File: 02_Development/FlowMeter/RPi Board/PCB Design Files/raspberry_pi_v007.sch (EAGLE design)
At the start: 136 parts, among them J3 277-2419-ND, J5 POWER_JACK, J7 277-2419-ND, J8 277-2419-ND, J9 277-2419-ND, P1 SPL006-007, P2 SPL006-007, P3 SPL006-007, P4 SPL006-007, P5 SPL006-007, Q1 4.3A/20V/54mΩ, Q2 500mA/300V, U1 P82B715TD, U5 P82B715TD, U6 TCA9548APWR, U7 TCA9548APWR, U8 P82B715TD, U9 P82B715TD

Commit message: Raspberry Pi PSV v007
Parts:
- removed ADC1: ADC128_8CH, th_libraries:ADC128_8CH
- added U2: TCA9548APWR, microbuilder:TCA9548A
- C10, C12: value 100nF -> 33n
- C11: value 100n -> 33n
- C14: value 1uF -> 470n
- C15: value 1uF -> 4.7pF; device SparkFun-Capacitors:CAP-0805 -> SparkFun-Capacitors:CAP-0603
- C16: value 33n -> 470nF
- C17: value 33n -> 100n
- C18: value 470n -> 10uF; device SparkFun-Capacitors:CAP-0805 -> microbuilder:CAP_CERAMIC0805-NOOUTLINE
- C2, C26, C30, C6: value 100nF -> 100n
- C21: value 330uF -> 100nF; device SparkFun-Capacitors:560UF-PANASONIC_G-25V-20% -> SparkFun-Capacitors:CAP-0805
- C22: value 22uF -> 100nF; device microbuilder:CAP_CERAMIC_1206 -> SparkFun-Capacitors:CAP-0805
- C23, C24: value 100nF -> 22uF; device SparkFun-Capacitors:CAP-0805 -> microbuilder:CAP_CERAMIC_1206
- C25: value 22uF -> 330uF; device microbuilder:CAP_CERAMIC_1206 -> SparkFun-Capacitors:560UF-PANASONIC_G-25V-20%
- C27: value 10uF -> 10u
- C28: value 470nF -> 100n
- C29: value 4.7pF -> 100nF; device SparkFun-Capacitors:CAP-0603 -> SparkFun-Capacitors:CAP-0805
- C3: value 100nF -> 1uF
- C4: value 33n -> 100nF
- C5: value 33n -> 1uF
- C7: value 10uF -> 100nF; device microbuilder:CAP_CERAMIC0805-NOOUTLINE -> SparkFun-Capacitors:CAP-0805
- C8: value 10u -> 33n; device microbuilder:CAP_CERAMIC0805-NOOUTLINE -> SparkFun-Capacitors:CAP-0805
- C9: value 100n -> 10uF; device SparkFun-Capacitors:CAP-0805 -> microbuilder:CAP_CERAMIC0805-NOOUTLINE
- J1, J2, J4: value (none) -> NP (277-2415-ND)
- J10: value (none) -> 277-2419-ND; device SparkFun-Connectors:CONN_02 -> th_libraries:CONN_043.5MM_RA
- J11: value (none) -> POWER_JACK; device SparkFun-Connectors:CONN_025MM -> SparkFun-Connectors:POWER_JACK
- J3: value 277-2419-ND -> NP (277-2415-ND); device th_libraries:CONN_043.5MM_RA -> SparkFun-Connectors:M03SCREW
- J5: value POWER_JACK -> 277-2419-ND; device SparkFun-Connectors:POWER_JACK -> th_libraries:CONN_043.5MM_RA
- J6: value (none) -> 277-2419-ND; device SparkFun-Connectors:M03SCREW -> th_libraries:CONN_043.5MM_RA
- J7: value 277-2419-ND -> 732-5315-ND; device th_libraries:CONN_043.5MM_RA -> SparkFun-Connectors:CONN_02
- J9: value 277-2419-ND -> 732-5315-ND; device th_libraries:CONN_043.5MM_RA -> SparkFun-Connectors:CONN_025MM
- Q1: value 4.3A/20V/54mΩ -> 500mA/300V; device SparkFun-DiscreteSemi:MOSFET_PCH-IRLML2244 -> SparkFun-DiscreteSemi:TRANS_NPN-MMBTA42
- Q2: value 500mA/300V -> 4.3A/20V/54mΩ; device SparkFun-DiscreteSemi:TRANS_NPN-MMBTA42 -> SparkFun-DiscreteSemi:MOSFET_PCH-IRLML2244
- R1, R2: value 470 -> 100; device SparkFun-Resistors:RESISTOR0805 -> SparkFun-Passives:RESISTOR0805-RES
- R11, R52: value 10K -> 2K; device SparkFun-Resistors:0.3OHM-0805-1/8W-1% -> SparkFun-Passives:RESISTOR0805-RES
- R12: value 2K -> 10K; device SparkFun-Passives:RESISTOR0805-RES -> SparkFun-Resistors:0.3OHM-0805-1/8W-1%
- R13, R16, R18, R31, R35: value 3K -> 10K
- R17, R29, R8: value 3K -> 100; device SparkFun-Resistors:0.3OHM-0805-1/8W-1% -> SparkFun-Passives:RESISTOR0805-RES
- R20, R40, R41, R42, R6: value 10K -> 3K
- R21: value 10k -> 3K
- R23: value 1K -> 10k; device SparkFun-Passives:RESISTOR0805-RES -> SparkFun-Resistors:0.3OHM-0805-1/8W-1%
- R24, R3: value 1K -> 100
- R25: value 10K -> 100; device SparkFun-Resistors:0.3OHM-0805-1/8W-1% -> SparkFun-Passives:RESISTOR0805-RES
- R26: value 100 -> 10K; device SparkFun-Passives:RESISTOR0805-RES -> SparkFun-Resistors:0.3OHM-0805-1/8W-1%
- R27: value 100 -> 49.9K
- R28: value 100 -> 365K
- R30: value 3K -> 470; device SparkFun-Resistors:0.3OHM-0805-1/8W-1% -> SparkFun-Resistors:RESISTOR0805
- R32: value 3K -> 100K; device SparkFun-Resistors:0.3OHM-0805-1/8W-1% -> SparkFun-Passives:RESISTOR0805-RES
- R36: value 3K -> 1K; device SparkFun-Resistors:0.3OHM-0805-1/8W-1% -> SparkFun-Passives:RESISTOR0805-RES
- R37, R38, R4, R43: value 100 -> 3K; device SparkFun-Passives:RESISTOR0805-RES -> SparkFun-Resistors:0.3OHM-0805-1/8W-1%
- R39: value 10K -> 470; device SparkFun-Resistors:0.3OHM-0805-1/8W-1% -> SparkFun-Resistors:RESISTOR0805
- R44: value 100 -> 470; device SparkFun-Passives:RESISTOR0805-RES -> SparkFun-Resistors:RESISTOR0805
- R45: value 1K -> 470; device SparkFun-Passives:RESISTOR0805-RES -> SparkFun-Resistors:RESISTOR0805
- R46: value 0 -> 10K
- R48: value 10K -> 0
- R49: value 365K -> 470; device SparkFun-Passives:RESISTOR0805-RES -> SparkFun-Resistors:RESISTOR0805
- R5: value 2K -> 3K; device SparkFun-Passives:RESISTOR0805-RES -> SparkFun-Resistors:0.3OHM-0805-1/8W-1%
- R50: value 49.9K -> 10K; device SparkFun-Passives:RESISTOR0805-RES -> SparkFun-Resistors:0.3OHM-0805-1/8W-1%
- R51: value 100K -> 10K; device SparkFun-Passives:RESISTOR0805-RES -> SparkFun-Resistors:0.3OHM-0805-1/8W-1%
- R53, R55, R56: value 470 -> 1K; device SparkFun-Resistors:RESISTOR0805 -> SparkFun-Passives:RESISTOR0805-RES
- U1: value P82B715TD -> ADC128_8CH; device Volks73-NXPSemiconductors:P82B715TD -> th_libraries:ADC128_8CH
- U6: value TCA9548APWR -> P82B715TD; device microbuilder:TCA9548A -> Volks73-NXPSemiconductors:P82B715TD
- renumbered D5 to D3, INDUCT to L1, REF1 to U3, RPI2 to RPI3B+, TPS to U4, U$15 to HOLE7, U$20 to TP4, U$23 to HOLE10, U$26 to HOLE1, U$31 to TP3, U$35 to HOLE9, U$36 to HOLE2, U$40 to TP1, U$45 to HOLE8, U$58 to HOLE3, U$59 to TP2, U$60 to HOLE4, U$61 to HOLE5, U$62 to HOLE6, U$64 to TP5
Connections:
- removed net N$10: Q2.B, R24.1, R48.2
- removed net N$11: C29.2, R49.1, R50.1, U4.VFB
- removed net N$12: ADC1.IN4, C1.1, R4.2
- removed net N$13: R11.2, R4.1, R5.1
- removed net N$14: C24.1, U4.VBST
- removed net N$15: D4.C, R23.2
- removed net N$16: D3.C, R45.2
- removed net N$17: R51.1, U4.PG
- removed net N$18: ADC1.IN0, C4.1, R26.1
- removed net N$19: ADC1.IN2, C5.1, R27.1
- removed net N$2: D2.C, R12.2
- removed net N$20: ADC1.IN1, C16.1, R28.1
- removed net N$22: ADC1.IN3, C17.1, R37.1
- removed net N$23: ADC1.SCLK, R38.2
- removed net N$24: ADC1.DOUT, R43.2
- removed net N$25: ADC1.DIN, R44.2
- removed net N$27: R52.2, U4.EN
- removed net N$6: C24.2, L1.1, U4.SW
- removed net N$7: C28.1, R51.2, U4.VREG
- removed net N$8: D1.C, R3.2
- removed net N$9: Q1.G, Q2.C, R47.1
- new net 12V-LED-R: D1.C, R52.2
- new net 3.3V-LED-R: D3.C, R55.2
- new net 5V-LED-R: D2.C, R53.2
- new net 5VREG-EN: R26.2, U4.EN
- new net 5VREG-PG: R32.1, U4.PG
- new net 5VREG-SW: C21.2, L1.1, U4.SW
- new net 5VREG-VBST: C21.1, U4.VBST
- new net 5VREG-VFB: C15.2, R27.1, R28.1, U4.VFB
- new net 5VREG-VREG: C16.1, R32.2, U4.VREG
- new net ADC-12V-SENSE: R11.1, R16.2, R17.1
- new net ADC-DIN: R29.2, U1.DIN
- new net ADC-DOUT: R25.2, U1.DOUT
- new net ADC-IN0: C11.1, R8.1, U1.IN0
- new net ADC-IN1: C10.1, R3.1, U1.IN1
- new net ADC-IN2: C8.1, R2.1, U1.IN2
- new net ADC-IN3: C1.1, R1.1, U1.IN3
- new net ADC-IN4: C12.1, R17.2, U1.IN4
- new net ADC-SCLK: R24.2, U1.SCLK
- new net PI5V-LED-R: D4.C, R56.2
- new net SENS_POWER_BASE: Q1.B, R35.2, R36.1
- new net SENS_POWER_GATE: Q1.C, Q2.G, R31.1
- net 00LX: now also J6.3, R44.1, U6U$1.LDA; no longer J7.3, R2.1, U1U$1.LDA
- net 00LY: now also J6.4, R45.1, U6U$1.LCL; no longer J7.4, R1.1, U1U$1.LCL
- net 00SCL: now also R38.1, U6U$1.SCL; no longer R30.1, U1U$1.SCL
- net 00SDA: now also R37.1, U6U$1.SDA; no longer R29.1, U1U$1.SDA
- net 0SCL: now also P5.SCK/SCL, R20.1, U2.SCL0; no longer P1.SCK/SCL, R8.1, U6.SCL0
- net 0SDA: now also P5.SDI/SDA, R21.1, U2.SDA0; no longer P1.SDI/SDA, R7.1, U6.SDA0
- net 11LX: now also J10.3, R57.1, U9U$1.LDA; no longer J3.3, R56.1, U8U$1.LDA
- net 11LY: now also J10.4, R58.1, U9U$1.LCL; no longer J3.4, R55.1, U8U$1.LCL
- net 11SCL: now also R43.1, U9U$1.SCL; no longer R32.1, U8U$1.SCL
- net 11SDA: now also R42.1, U9U$1.SDA; no longer R31.1, U8U$1.SDA
- net 12V: now also C18.1, C22.1, C25.+, D1.A, J11.PWR, J3.1, R16.1, R26.1; no longer C20.1, C21.+, C27.1, D2.A, J5.PWR, J6.1, R11.1, R52.1
- net 1SCL: now also P4.SCK/SCL, R14.1, U2.SCL1; no longer P2.SCK/SCL, R10.1, U6.SCL1
- net 1SDA: now also P4.SDI/SDA, R15.1, U2.SDA1; no longer P2.SDI/SDA, R9.1, U6.SDA1
- net 22LX: now also R49.1, U8U$1.LDA; no longer R58.1, U9U$1.LDA
- net 22LY: now also R54.1, U8U$1.LCL; no longer R57.1, U9U$1.LCL
- net 22SCL: now also R40.1, U8U$1.SCL; no longer R34.1, U9U$1.SCL
- net 22SDA: now also R41.1, U8U$1.SDA; no longer R33.1, U9U$1.SDA
- net 2SCL: now also R9.1, U2.SCL2; no longer R14.1, U6.SCL2
- net 2SDA: now also R10.1, U2.SDA2; no longer R13.1, U6.SDA2
- net 3.3V: now also C13.1, C20.1, C27.1, C29.1, C4.1, C5.1, R19.1, R20.2, R23.2, R35.1, R4.2, R46.2, R5.2, R50.1, R6.2, U1.VD, U2.VCC; no longer ADC1.VD, C10.1, C12.1, C15.1, C2.1, C3.1, C8.1, R13.2, R16.2, R17.2, R18.2, R41.2, R42.1, R48.1, R6.1, R8.2, U6.VCC
- net 33LX: now also J5.3, R30.1; no longer J9.3, R54.1
- net 33LY: now also J5.4, R39.1; no longer J9.4, R53.1
- net 33SCL: now also R33.1; no longer R36.1
- net 33SDA: now also R34.1; no longer R35.1
- net 3SCL: now also P1.SCK/SCL, R6.1, U2.SCL3; no longer P4.SCK/SCL, R16.1, U6.SCL3
- net 3SDA: now also P1.SDI/SDA, R7.1, U2.SDA3; no longer P4.SDI/SDA, R15.1, U6.SDA3
- net 4.096V: now also C2.1, C3.1, U1.VA; no longer ADC1.VA, C11.1, C14.1
- net 4SCL: now also P2.SCK/SCL, R4.1, U2.SCL4; no longer P5.SCK/SCL, R18.1, U6.SCL4
- net 4SDA: now also P2.SDI/SDA, R5.1, U2.SDA4; no longer P5.SDI/SDA, R17.1, U6.SDA4
- net 5V: now also C15.1, C23.1, C24.1, D2.A, J7.2, R28.2; no longer C22.1, C25.1, C29.1, D4.A, J10.2, R49.2
- net A0_PC: now also R13.1, U2.A0; no longer R19.1, U6.A0
- net A1_PC: now also R18.1, U2.A1; no longer R20.1, U6.A1
- net A2_PC: now also R12.1, U2.A2; no longer R25.1, U6.A2
- net A3_PC: now also R51.1; no longer R39.1
- net A4_PC: now also R47.1; no longer R40.1
- net A5_PC: now also R46.1; no longer R41.1
- net ADC1: now also J4.3, R8.2; no longer J1.3, R26.2
- net ADC2: now also J3.3, R3.2; no longer J2.3, R28.2
- net ADC3: now also J2.3, R2.2; no longer J4.3, R27.2
- net ADC4: now also J1.3, R1.2; no longer J6.3, R37.2
- net GND: now also C24.2, C25.-, C29.2, J10.2, J11.GND, J11.GNDBREAK, J5.2, J9.1, Q1.E, R11.2, R12.2, R13.2, R18.2, R27.2, R47.2, R48.2, R51.2, R52.1, R53.1, R55.1, R56.1, U1.AGND, U1.CS, U1.DGND, U2.GND, U6-SUPPLY.GND; no longer ADC1.AGND, ADC1.CS, ADC1.DGND, C15.2, C21.-, C25.2, J11.1, J5.GND, J5.GNDBREAK, J7.2, J9.2, Q2.E, R12.1, R19.2, R20.2, R23.1, R25.2, R3.1, R39.2, R40.2, R45.1, R46.2, R5.2, R50.2, U1-SUPPLY.GND, U6.GND
- net GND1: now also R48.1; no longer R46.1
- net GPIO12: now also R36.2; no longer R24.2
- net PI_5V_POWER: now also C14.1, D4.A, J7.1, J9.2, Q2.S, R31.2; no longer C18.1, D1.A, J10.1, J11.2, Q1.S, R47.2
- net RESET: now also R19.2, R50.2, U2.#RESET; no longer R42.2, R6.2, U6.#RESET
- net SCL: now also U2.SCL; no longer U6.SCL
- net SDA: now also R23.1, U2.SDA; no longer R21.1, U6.SDA
- net SENS_POWER: now also C17.1, C28.1, J10.1, J5.1, J6.1, Q2.D, R37.2, R38.2, R39.2, R40.2, R41.2, R42.2, R43.2, R44.2, R45.2, R49.2, U6-SUPPLY.VCC; no longer C13.1, C23.1, J3.1, J7.1, J9.1, Q1.D, R1.2, R2.2, R29.2, R31.2, R32.2, R35.2, R36.2, R53.2, R55.2, R56.2, U1-SUPPLY.VCC
- net SPI_MISO: now also R25.1; no longer R43.1
- net SPI_MOSI: now also R29.1; no longer R44.1
- net SPI_SCLK: now also R24.1; no longer R38.1
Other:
- note added: "version 007 01/01/2021 editor P CAMPBELL - Added missing part numbers, renumbered - Cleaned up ERC with approvals - Cleaned up Net Names - Layout cleanup (extensive) version 006 31/12/2020 editor P CAMPBELL - Added I2C bus extenders on Sensirion - Changed I2C pullups on Sensirion from 3.3V to 5V version 005 14/12/2020 editor Darragh Broadbent - changed pull up resistor value between I2C multiplex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"
- note removed: "version 006 31/12/2020 editor P CAMPBELL - Added I2C bus extenders on Sensirion - Changed I2C pullups on Sensirion from 3.3V to 5V version 005 14/12/2020 editor Darragh Broadbent - changed pull up resistor value between I2C multiplexer and slave devices to 3K from 10K - resolved clearance issues version 004 12/5/2020 - add new 5V regulator version 003 - removed piezo buzzer - used transistor/P-ch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"
- moved on the sheet: C1, C10, C11, C12, C13, C14, C15, C16, C17, C18, C2, C20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

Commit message: v007 documentation updates & manufacturing files
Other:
- note added: "Q1 Transistor MFR Part# S8050 LCSC Part# C2146 Package SOT-23-3 NPN 500MA 25V https://datasheet.lcsc.com/szlcsc/Changjiang-Electronics-Tech-CJ-S8050_C2146.pdf 1-base, 2-emitter, 3-collector Q2 P-ch Mosfet MFR Part# AO3401A LCSC Part# C15127 Package SOT-23-3 https://datasheet.lcsc.com/szlcsc/Alpha-Omega-Semicon-AOS-AO3401A_C15127.pdf 1-gate, 2-source, 3-drain"
- note added: "version 007b 03/01/2021 editor P CAMPBELL - Changed note on Q1 & Q2 DOCUMENTATION CHANGE ONLY version 007 01/01/2021 editor P CAMPBELL - Added missing part numbers, renumbered - Cleaned up ERC with approvals - Cleaned up Net Names - Layout cleanup (extensive) version 006 31/12/2020 editor P CAMPBELL - Added I2C bus extenders on Sensirion - Changed I2C pullups on Sensirion from 3.3V to 5V version 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"
- note removed: "Q1 P-ch Mosfet MFR Part# AO3401A LCSC Part# C15127 Package SOT-23-3 https://datasheet.lcsc.com/szlcsc/Alpha-Omega-Semicon-AOS-AO3401A_C15127.pdf 1-gate, 2-source, 3-drain Q2 Transistor MFR Part# S8050 LCSC Part# C2146 Package SOT-23-3 NPN 500MA 25V https://datasheet.lcsc.com/szlcsc/Changjiang-Electronics-Tech-CJ-S8050_C2146.pdf 1-base, 2-emitter, 3-collector"
- note removed: "version 007 01/01/2021 editor P CAMPBELL - Added missing part numbers, renumbered - Cleaned up ERC with approvals - Cleaned up Net Names - Layout cleanup (extensive) version 006 31/12/2020 editor P CAMPBELL - Added I2C bus extenders on Sensirion - Changed I2C pullups on Sensirion from 3.3V to 5V version 005 14/12/2020 editor Darragh Broadbent - changed pull up resistor value between I2C multiplex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"
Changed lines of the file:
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@@
 https://datasheet.lcsc.com/szlcsc/Texas-Instruments-TI-REF3040AIDBZR_C19415.pdf
 </text>
-<text x="190.5" y="0" size="1.778" layer="91" align="top-left">Q1 P-ch Mosfet
-MFR Part# AO3401A
-LCSC Part# C15127
-Package SOT-23-3
-https://datasheet.lcsc.com/szlcsc/Alpha-Omega-Semicon-AOS-AO3401A_C15127.pdf
-1-gate, 2-source, 3-drain
-Q2 Transistor
+<text x="190.5" y="0" size="1.778" layer="91" align="top-left">Q1 Transistor
 MFR Part# S8050
 LCSC Part# C2146
@@
 https://datasheet.lcsc.com/szlcsc/Changjiang-Electronics-Tech-CJ-S8050_C2146.pdf
 1-base, 2-emitter, 3-collector
+Q2 P-ch Mosfet
+MFR Part# AO3401A
+LCSC Part# C15127
+Package SOT-23-3
+https://datasheet.lcsc.com/szlcsc/Alpha-Omega-Semicon-AOS-AO3401A_C15127.pdf
+1-gate, 2-source, 3-drain
 </text>
 <text x="3.048" y="110.49" size="1.778" layer="91" align="top-left">Input Voltage
@@
 - - 12VDC/5DC converter is active, jumper is made and RPI,Display, and peripherials powered by converter
 Scenario #4 - </text>
-<text x="-125.476" y="183.388" size="1.778" layer="91">version 007 01/01/2021 editor P CAMPBELL
+<text x="-125.476" y="183.388" size="1.778" layer="91">version 007b 03/01/2021 editor P CAMPBELL
+- Changed note on Q1 &amp; Q2
+DOCUMENTATION CHANGE ONLY
+version 007 01/01/2021 editor P CAMPBELL
 - Added missing part numbers, renumbered
 - Cleaned up ERC with approvals

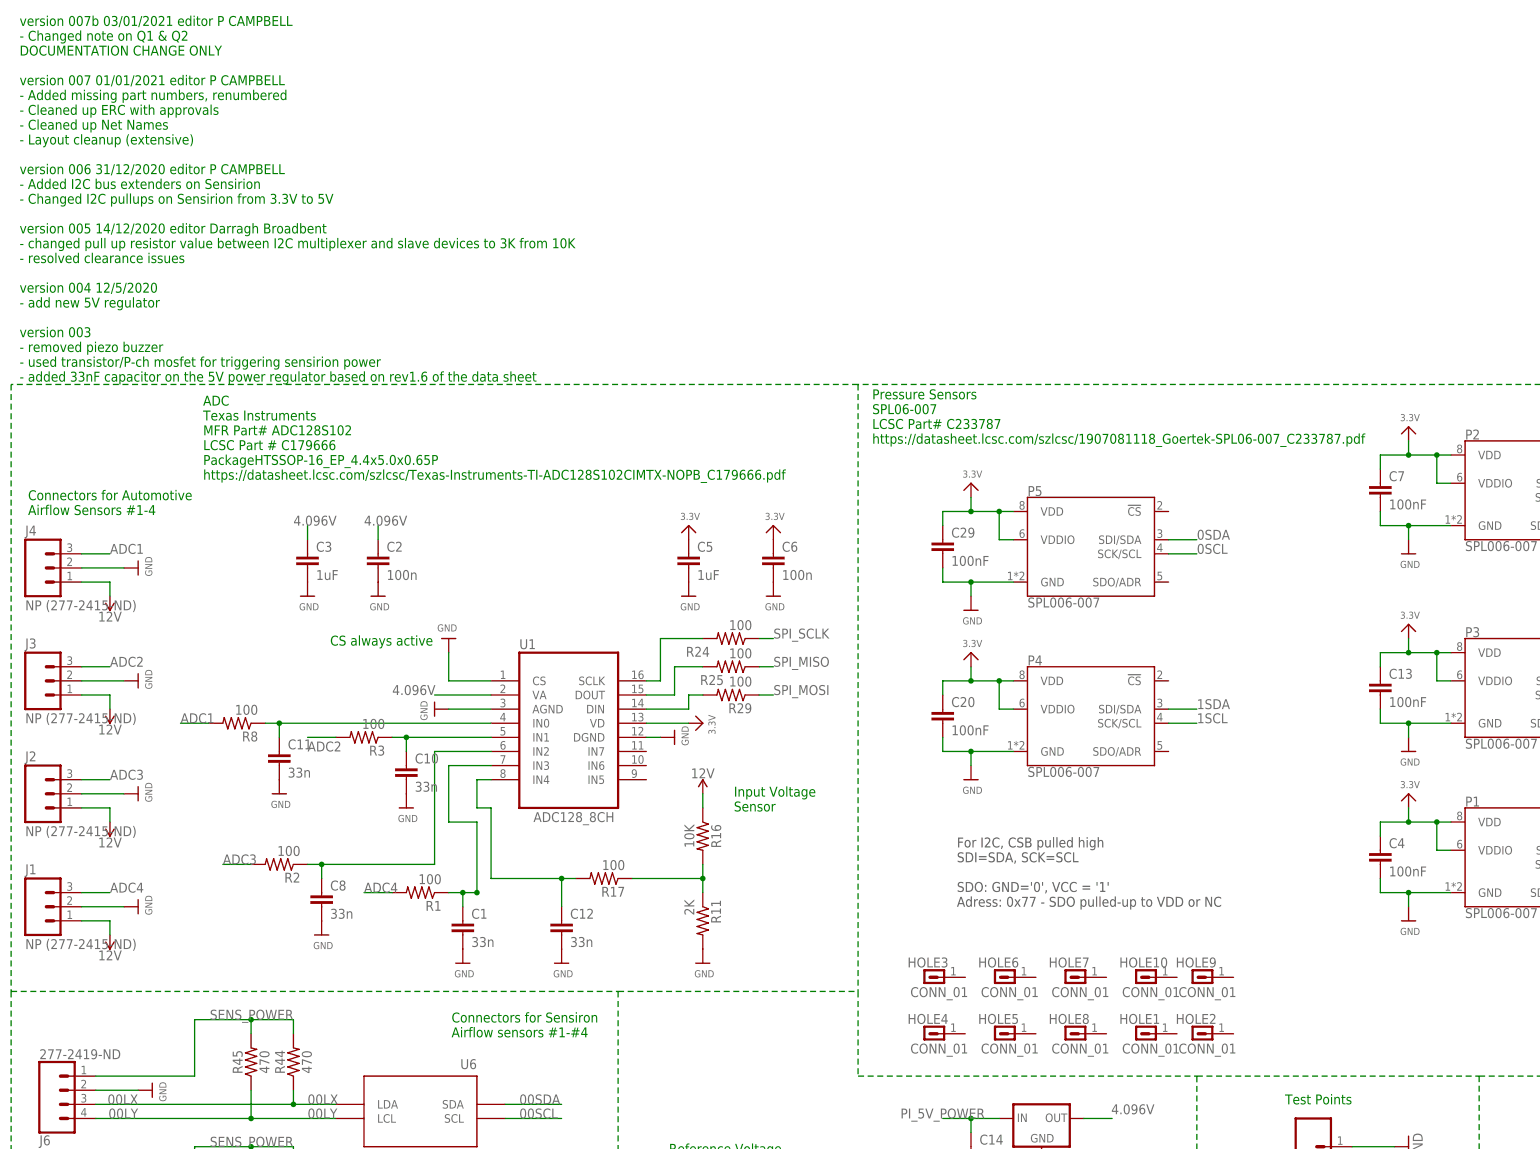
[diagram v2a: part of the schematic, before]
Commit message: add fiducials & CAD step file, cleanup
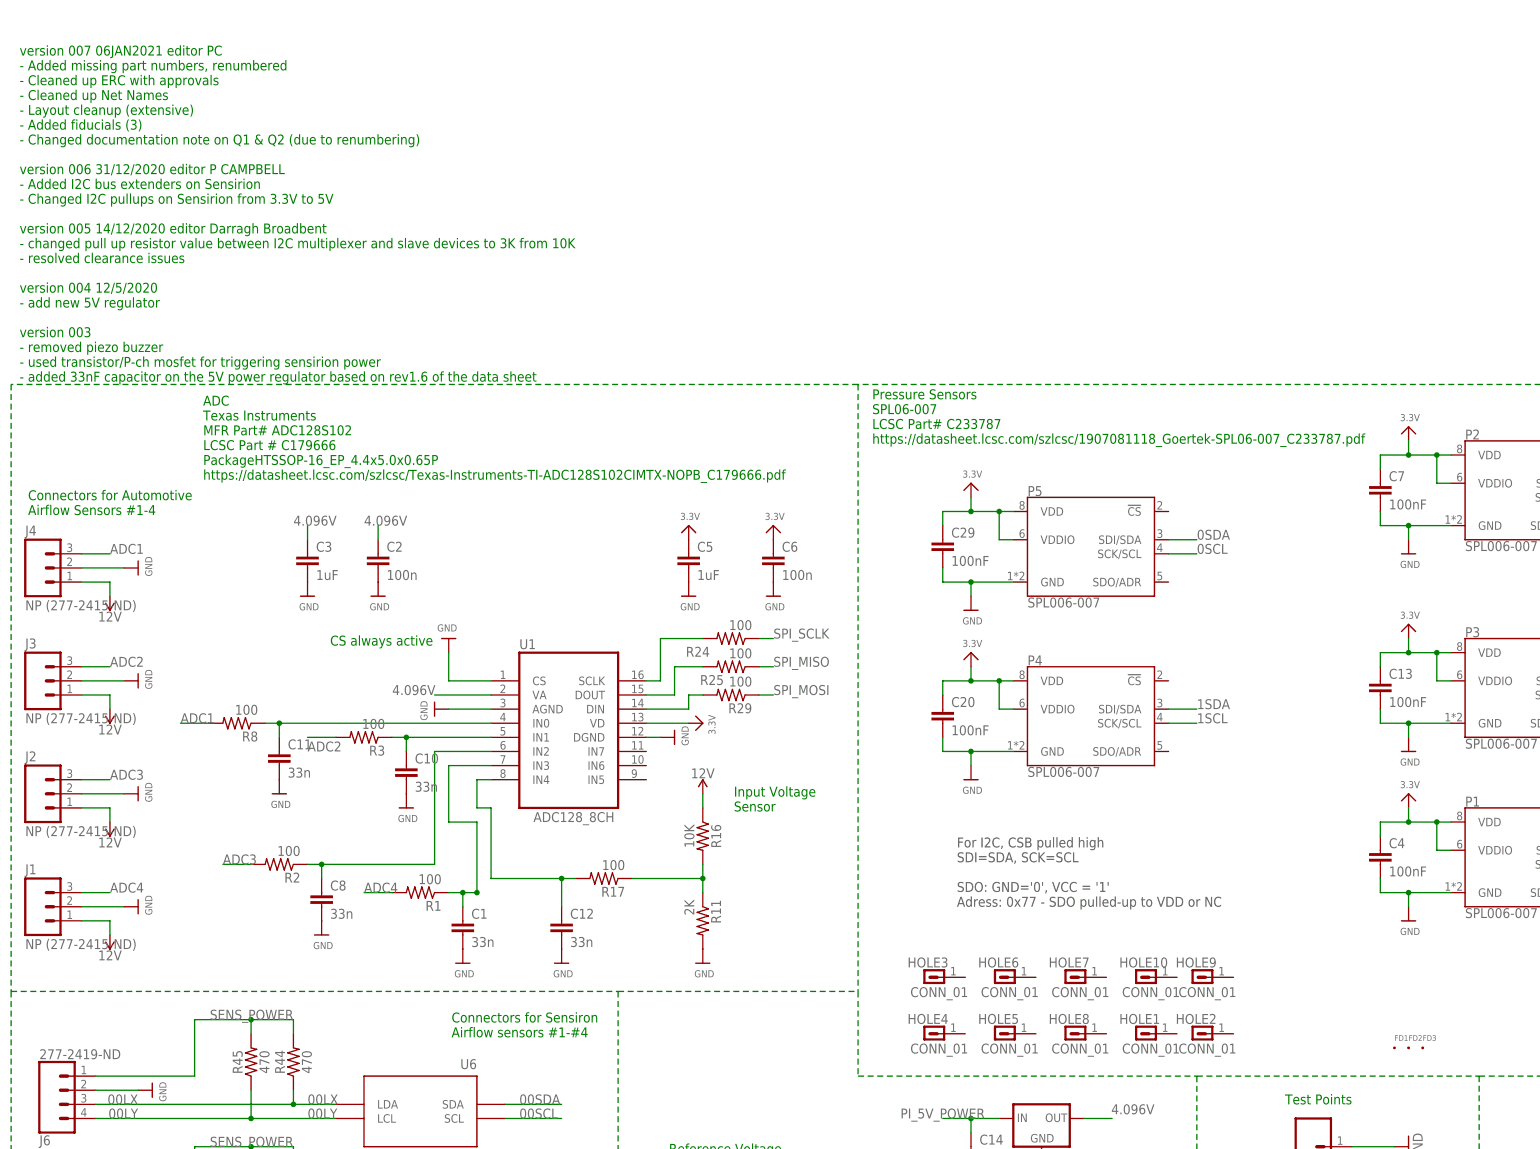
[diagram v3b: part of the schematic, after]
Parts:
- added FD1, FD2, FD3: FID_40MIL, Fiducial:FID_40MIL
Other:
- note added: "version 007 06JAN2021 editor PC - Added missing part numbers, renumbered - Cleaned up ERC with approvals - Cleaned up Net Names - Layout cleanup (extensive) - Added fiducials (3) - Changed documentation note on Q1 & Q2 (due to renumbering) version 006 31/12/2020 editor P CAMPBELL - Added I2C bus extenders on Sensirion - Changed I2C pullups on Sensirion from 3.3V to 5V version 005 14/12/2020 edito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"
- note removed: "version 007b 03/01/2021 editor P CAMPBELL - Changed note on Q1 & Q2 DOCUMENTATION CHANGE ONLY version 007 01/01/2021 editor P CAMPBELL - Added missing part numbers, renumbered - Cleaned up ERC with approvals - Cleaned up Net Names - Layout cleanup (extensive) version 006 31/12/2020 editor P CAMPBELL - Added I2C bus extenders on Sensirion - Changed I2C pullups on Sensirion from 3.3V to 5V version 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"
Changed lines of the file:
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@@
 <part name="U$67" library="microbuilder" deviceset="GND" device=""/>
 <part name="U$77" library="microbuilder" deviceset="GND" device=""/>
+<part name="FD1" library="Fiducial" deviceset="FID" device="_40MIL"/>
+<part name="FD2" library="Fiducial" deviceset="FID" device="_40MIL"/>
+<part name="FD3" library="Fiducial" deviceset="FID" device="_40MIL"/>
 </parts>
 <sheets>
@@
 - - 12VDC/5DC converter is active, jumper is made and RPI,Display, and peripherials powered by converter
 Scenario #4 - </text>
-<text x="-125.476" y="183.388" size="1.778" layer="91">version 007b 03/01/2021 editor P CAMPBELL
-- Changed note on Q1 &amp; Q2
-DOCUMENTATION CHANGE ONLY
-version 007 01/01/2021 editor P CAMPBELL
+<text x="-125.476" y="183.388" size="1.778" layer="91">version 007 06JAN2021 editor PC
 - Added missing part numbers, renumbered
 - Cleaned up ERC with approvals
 - Cleaned up Net Names
 - Layout cleanup (extensive)
+- Added fiducials (3)
+- Changed documentation note on Q1 &amp; Q2 (due to renumbering)
 version 006 31/12/2020 editor P CAMPBELL
 - Added I2C bus extenders on Sensirion
@@
 <attribute name="VALUE" x="54.356" y="-35.56" size="1.27" layer="96"/>
 </instance>
+<instance part="FD1" gate="G$2" x="121.92" y="63.5" smashed="yes">
+<attribute name="NAME" x="121.92" y="64.77" size="1.016" layer="95" font="vector" ratio="12"/>
+</instance>
+<instance part="FD2" gate="G$2" x="124.46" y="63.5" smashed="yes">
+<attribute name="NAME" x="124.46" y="64.77" size="1.016" layer="95" font="vector" ratio="12"/>
+</instance>
+<instance part="FD3" gate="G$2" x="127" y="63.5" smashed="yes">
+<attribute name="NAME" x="127" y="64.77" size="1.016" layer="95" font="vector" ratio="12"/>
+</instance>
 </instances>
